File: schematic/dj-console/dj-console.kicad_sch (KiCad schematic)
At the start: 21 parts, among them U37 LM741, U38 MCP3204, U39 LM741, U40 LM741

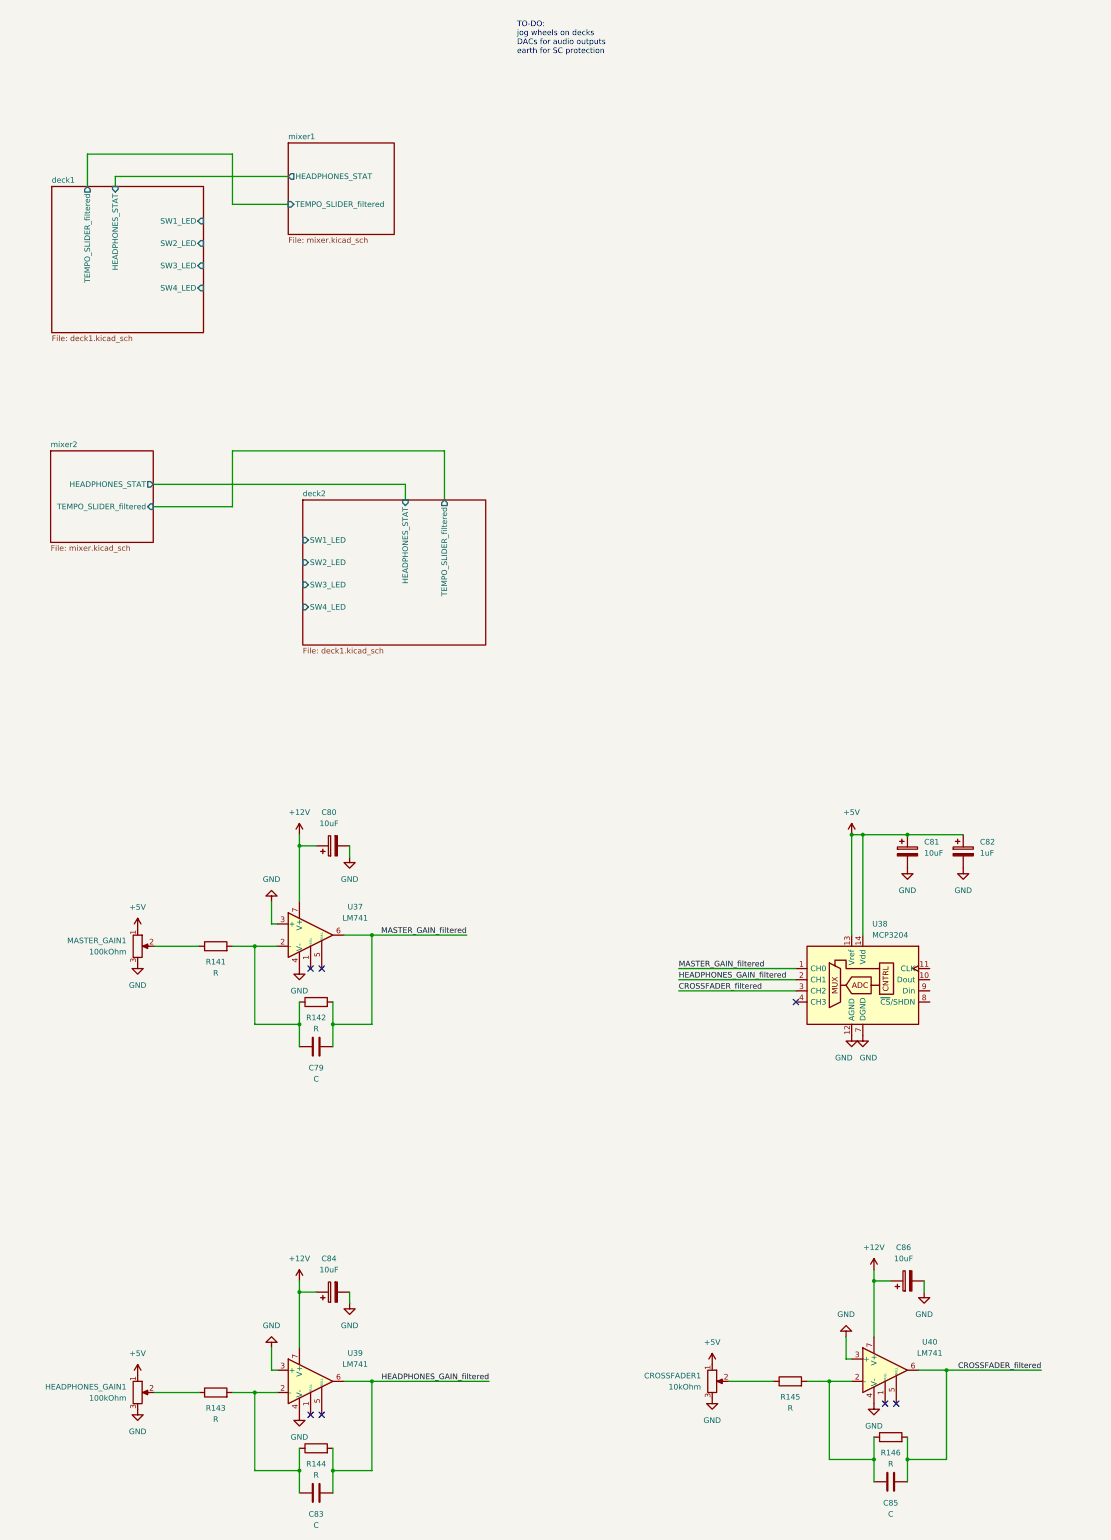
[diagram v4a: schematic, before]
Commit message: Changed filtering circuit for knobs
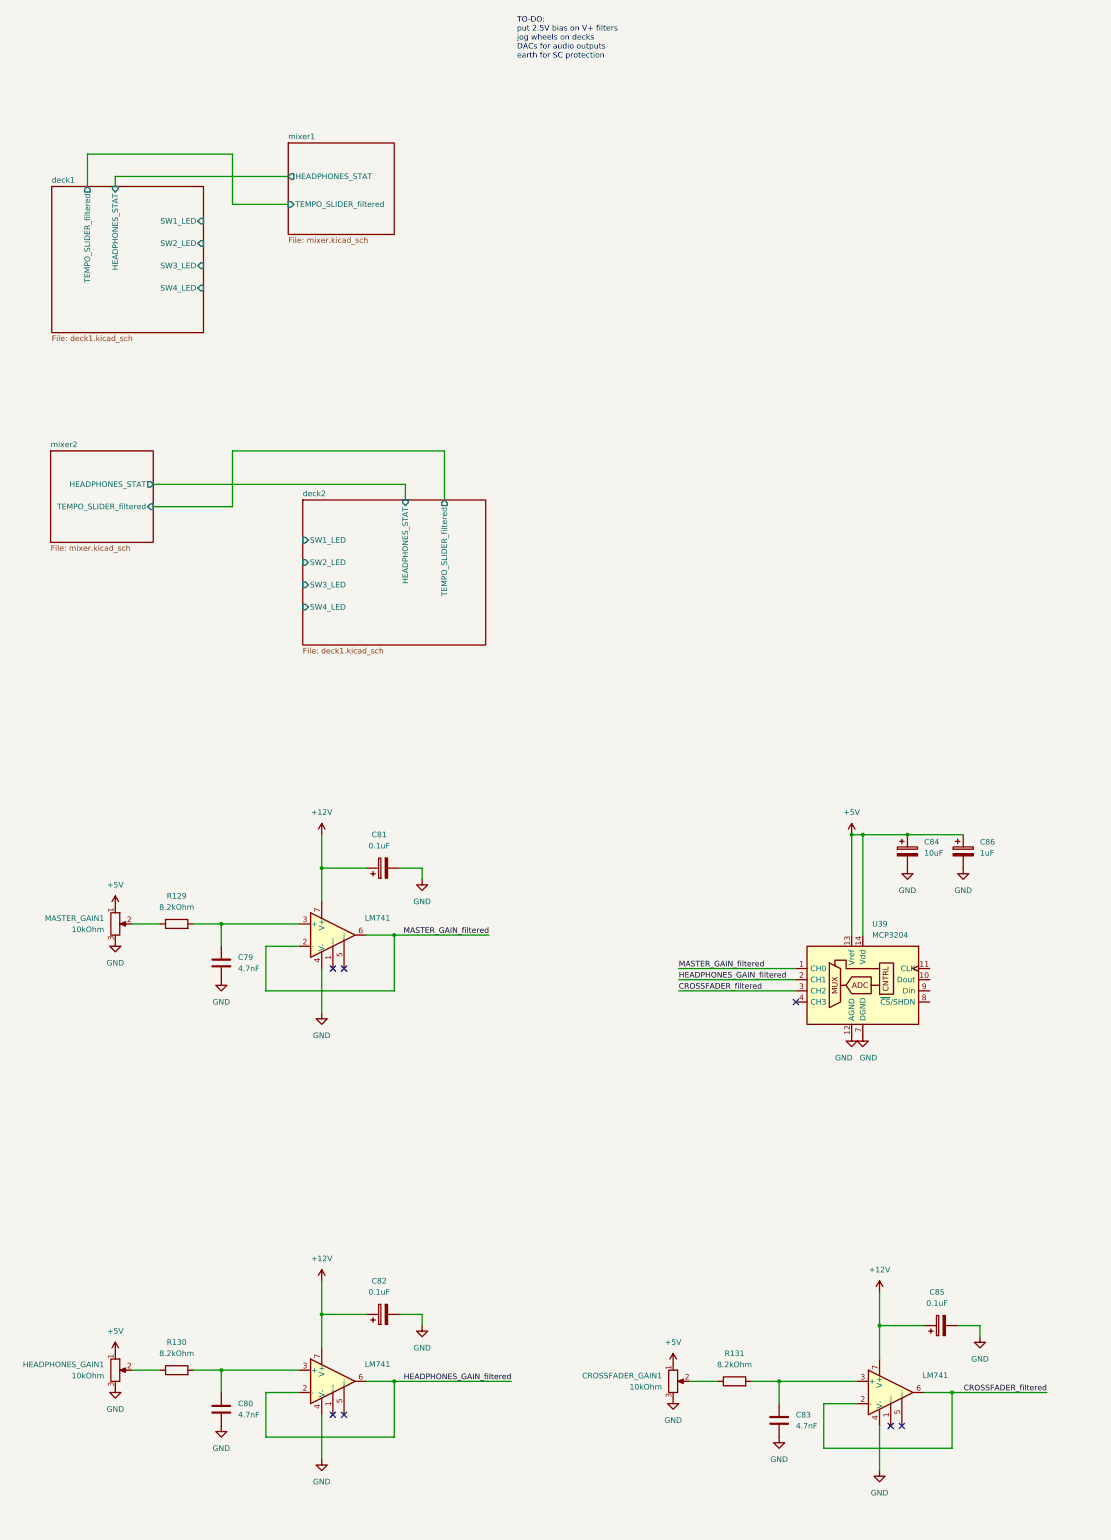
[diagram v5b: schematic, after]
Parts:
- removed C80, C84, C86: 10uF, symbol Device:C_Polarized
- removed C85: C, symbol Device:C
- removed CROSSFADER1: 10kOhm, symbol Device:R_Potentiometer
- removed R141, R142, R143, R144, R145, R146: R, symbol Device:R
- removed U39: LM741, symbol Amplifier_Operational:LM741
- added C80: 4.7nF, symbol Device:C
- added C81, C82, C85: 0.1uF, symbol Device:C_Polarized
- added CROSSFADER_GAIN1: 10kOhm, symbol Device:R_Potentiometer
- added R129, R130, R131: 8.2kOhm, symbol Device:R
- added U38: LM741, symbol Amplifier_Operational:LM741
- C79, C83: value C -> 4.7nF
- HEADPHONES_GAIN1, MASTER_GAIN1: value 100kOhm -> 10kOhm
- renumbered C81 to C84, C82 to C86, U38 to U39
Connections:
- net +12V: now also C81.1, C82.1, C85.1, U38.7 (V+)
- net +5V: now also CROSSFADER_GAIN1.1
- net CROSSFADER_filtered: now also U40.2 (-)
- net GND: now also C79.2, C83.2, C80.2, C81.2, C82.2, C85.2, CROSSFADER_GAIN1.3, U38.4 (V-); no longer U37.3 (+), U40.3 (+)
- net HEADPHONES_GAIN_filtered: now also U38.2 (-), U38.6; no longer C83.1
- net MASTER_GAIN_filtered: now also U37.2 (-); no longer C79.1
- net at HEADPHONES_GAIN1.2: now also R130.1
- net at MASTER_GAIN1.2: now also R129.1
- new net: C80.1, R130.2, U38.3 (+)
- new net: C83.1, R131.2, U40.3 (+)
- new net: CROSSFADER_GAIN1.2, R131.1
- new net: C79.1, R129.2, U37.3 (+)
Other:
- note added: "TO-DO: put 2.5V bias on V+ filters jog wheels on decks DACs for audio outputs earth for SC protection"
- note removed: "TO-DO: jog wheels on decks DACs for audio outputs earth for SC protection"

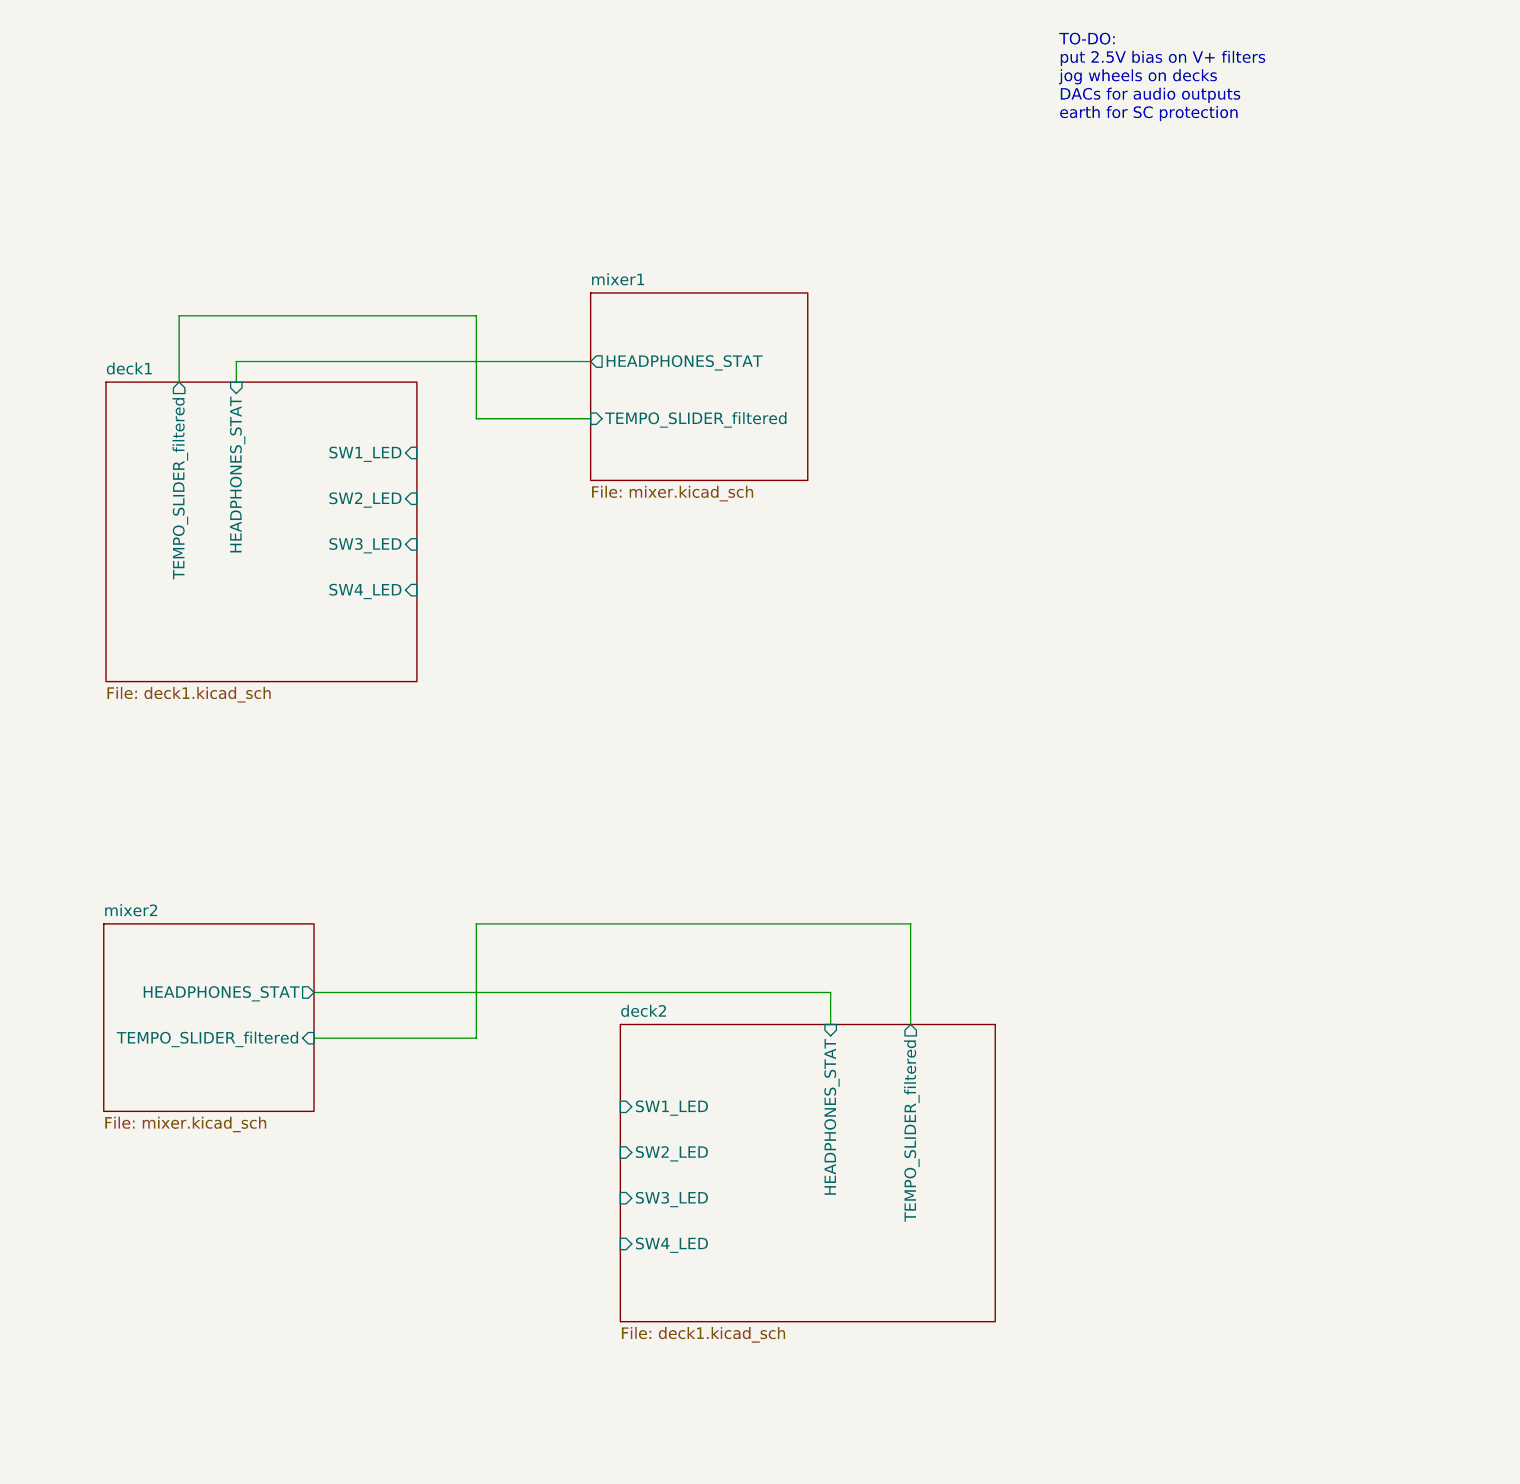
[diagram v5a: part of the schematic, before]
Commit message: Added I2C and SPI busses
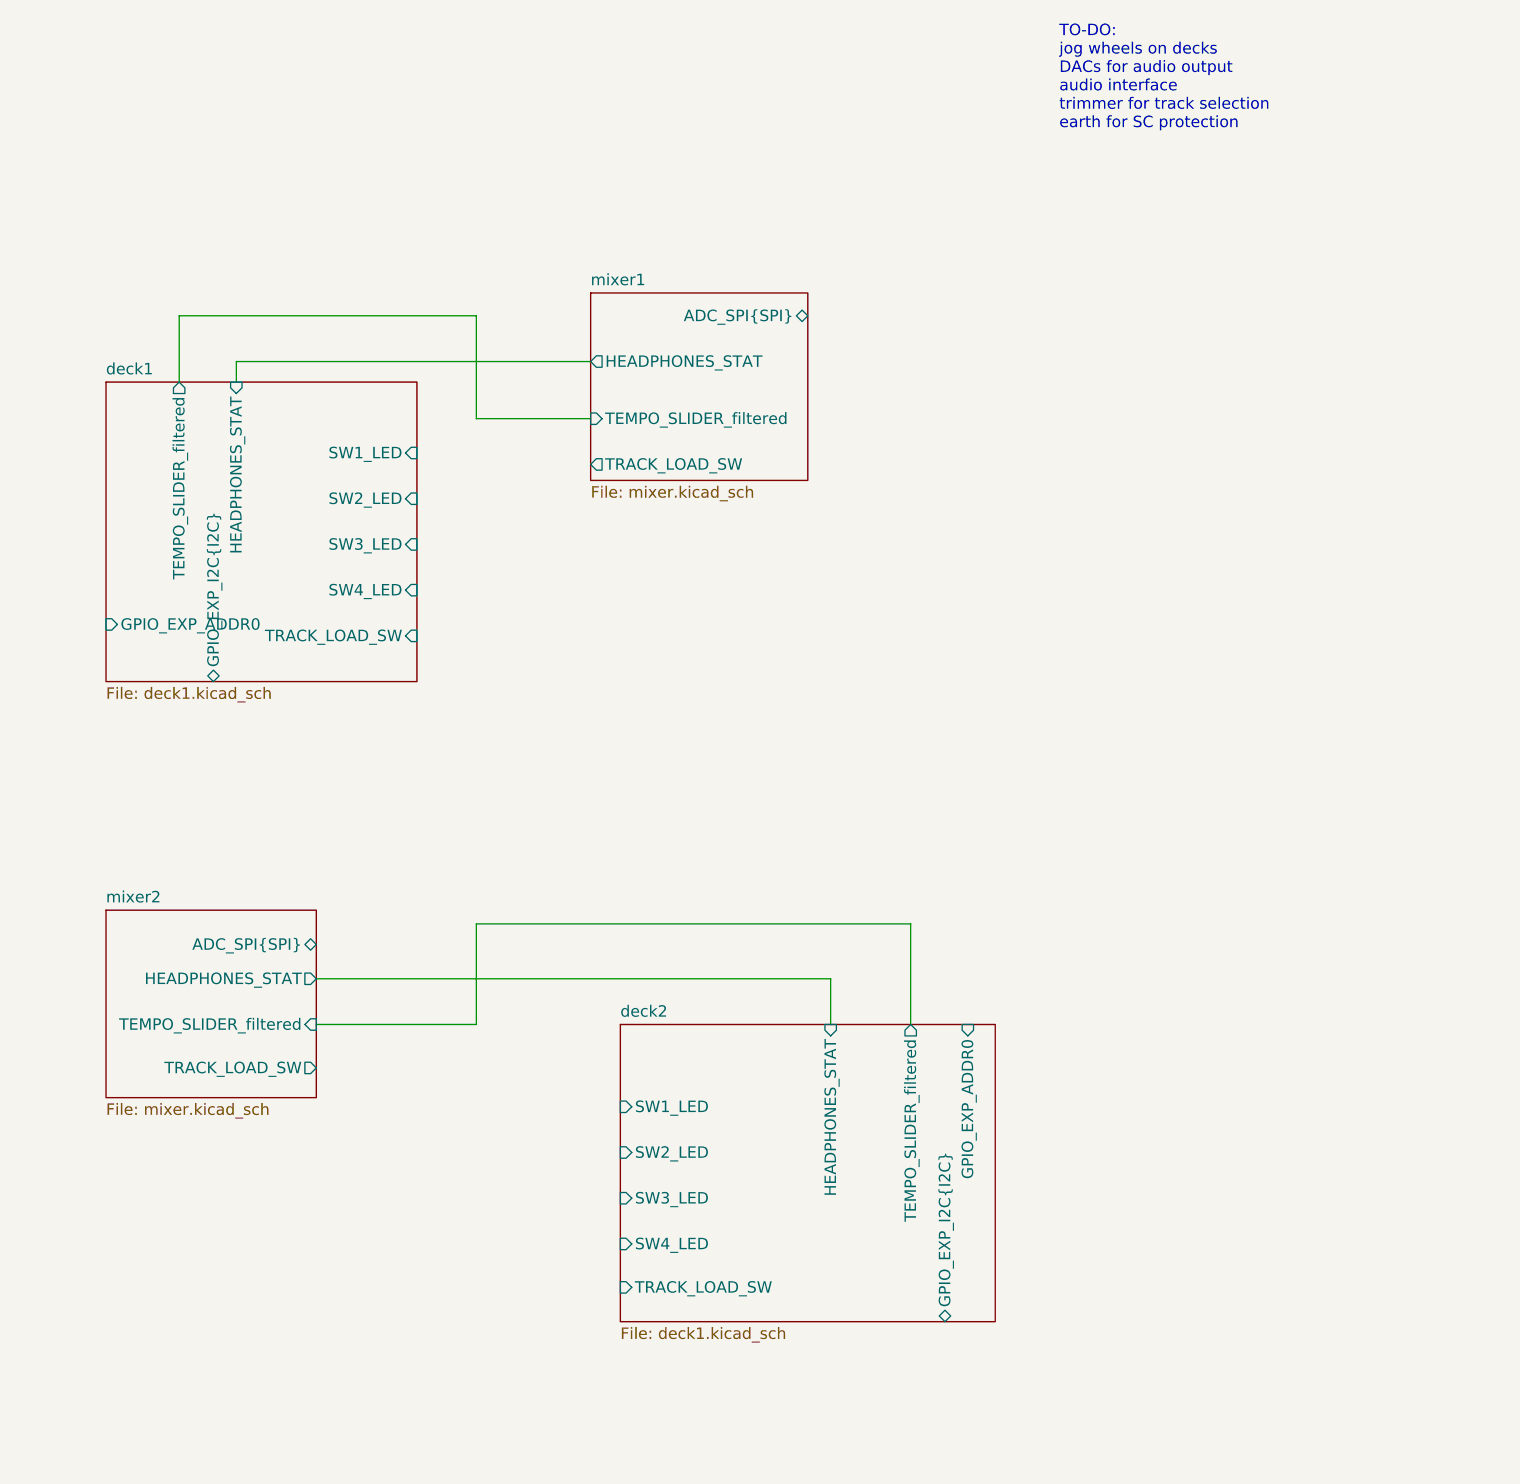
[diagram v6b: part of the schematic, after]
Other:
- sheet deck1 ports: added GPIO_EXP_ADDR0, GPIO_EXP_I2C{I2C}, TRACK_LOAD_SW; removed none
- sheet deck2 ports: added GPIO_EXP_ADDR0, GPIO_EXP_I2C{I2C}, TRACK_LOAD_SW; removed none
- sheet mixer1 ports: added ADC_SPI{SPI}, TRACK_LOAD_SW; removed none
- sheet mixer2 ports: added ADC_SPI{SPI}, TRACK_LOAD_SW; removed none
- note added: "TO-DO: jog wheels on decks DACs for audio output audio interface trimmer for track selection earth for SC protection"
- note removed: "TO-DO: put 2.5V bias on V+ filters jog wheels on decks DACs for audio outputs earth for SC protection"
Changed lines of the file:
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@@
 		(company "Loris Panaro")
 	)
-	(text "TO-DO: \nput 2.5V bias on V+ filters\njog wheels on decks\nDACs for audio outputs\nearth for SC protection\n"
+	(text "TO-DO: \njog wheels on decks\nDACs for audio output\naudio interface\ntrimmer for track selection\nearth for SC protection\n"
 		(exclude_from_sim no)
 		(at 128.27 24.384 0)
@@
 	(wire
 		(pts
-			(xy 45.466 131.064) (xy 63.5 131.064)
+			(xy 45.72 129.54) (xy 63.5 129.54)
 		)
 		(stroke
@@
 	(wire
 		(pts
-			(xy 63.5 131.064) (xy 63.5 118.364)
+			(xy 63.5 129.54) (xy 63.5 118.364)
 		)
 		(stroke
@@
 	(wire
 		(pts
-			(xy 102.87 125.984) (xy 102.87 129.54)
+			(xy 102.87 124.46) (xy 102.87 129.54)
 		)
 		(stroke
@@
 	(wire
 		(pts
-			(xy 45.466 125.984) (xy 102.87 125.984)
+			(xy 45.72 124.46) (xy 102.87 124.46)
 		)
 		(stroke
@@
 			)
 		)
+		(pin "TRACK_LOAD_SW" input
+			(at 79.502 158.75 180)
+			(effects
+				(font
+					(size 1.27 1.27)
+				)
+				(justify left)
+			)
+		)
+		(pin "GPIO_EXP_I2C{I2C}" bidirectional
+			(at 115.57 162.56 270)
+			(effects
+				(font
+					(size 1.27 1.27)
+				)
+				(justify left)
+			)
+		)
+		(pin "GPIO_EXP_ADDR0" input
+			(at 118.11 129.54 90)
+			(effects
+				(font
+					(size 1.27 1.27)
+				)
+				(justify right)
+			)
+		)
 		(instances
 			(project "dj-console"
@@
 			)
 		)
+		(pin "TRACK_LOAD_SW" output
+			(at 76.2 67.31 180)
+			(effects
+				(font
+					(size 1.27 1.27)
+				)
+				(justify left)
+			)
+		)
+		(pin "ADC_SPI{SPI}" bidirectional
+			(at 100.33 50.8 0)
+			(effects
+				(font
+					(size 1.27 1.27)
+				)
+				(justify right)
+			)
+		)
 		(instances
 			(project "dj-console"
@@
 	)
 	(sheet
-		(at 22.098 118.364)
+		(at 22.352 116.84)
 		(size 23.368 20.828)
 		(exclude_from_sim no)
@@
 		)
 		(property "Sheetname" "mixer2"
-			(at 22.098 117.6524 0)
+			(at 22.352 116.1284 0)
 			(show_name no)
 			(do_not_autoplace no)
@@
 		)
 		(property "Sheetfile" "mixer.kicad_sch"
-			(at 22.098 139.7766 0)
+			(at 22.352 138.2526 0)
 			(show_name no)
 			(do_not_autoplace no)
@@
 		)
 		(pin "HEADPHONES_STAT" output
-			(at 45.466 125.984 0)
+			(at 45.72 124.46 0)
 			(effects
 				(font
@@
 		)
 		(pin "TEMPO_SLIDER_filtered" input
-			(at 45.466 131.064 0)
+			(at 45.72 129.54 0)
+			(effects
+				(font
+					(size 1.27 1.27)
+				)
+				(justify right)
+			)
+		)
+		(pin "TRACK_LOAD_SW" output
+			(at 45.72 134.366 0)
+			(effects
+				(font
+					(size 1.27 1.27)
+				)
+				(justify right)
+			)
+		)
+		(pin "ADC_SPI{SPI}" bidirectional
+			(at 45.72 120.65 0)
 			(effects
 				(font
@@
 			)
 		)
+		(pin "TRACK_LOAD_SW" input
+			(at 56.896 86.36 0)
+			(effects
+				(font
+					(size 1.27 1.27)
+				)
+				(justify right)
+			)
+		)
+		(pin "GPIO_EXP_I2C{I2C}" bidirectional
+			(at 34.29 91.44 270)
+			(effects
+				(font
+					(size 1.27 1.27)
+				)
+				(justify left)
+			)
+		)
+		(pin "GPIO_EXP_ADDR0" input
+			(at 22.352 85.09 180)
+			(effects
+				(font
+					(size 1.27 1.27)
+				)
+				(justify left)
+			)
+		)
